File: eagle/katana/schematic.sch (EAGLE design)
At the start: 27 parts, among them IC1 MAX1044, Q1 2N5457, Q2 2N5457

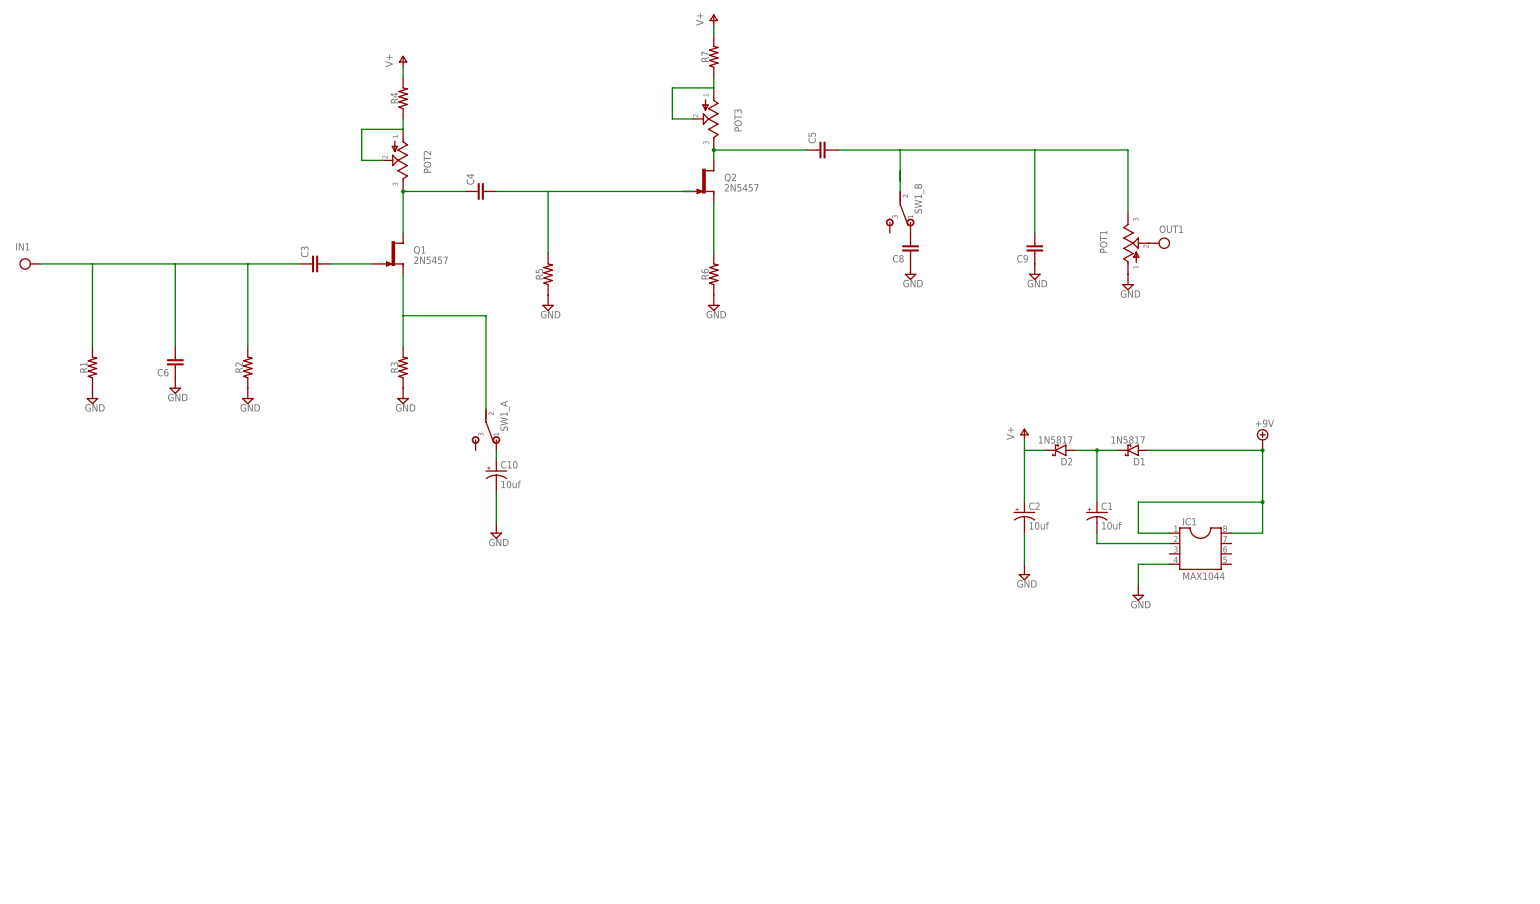
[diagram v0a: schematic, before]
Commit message: Se ha modificado esquematico y creado layout
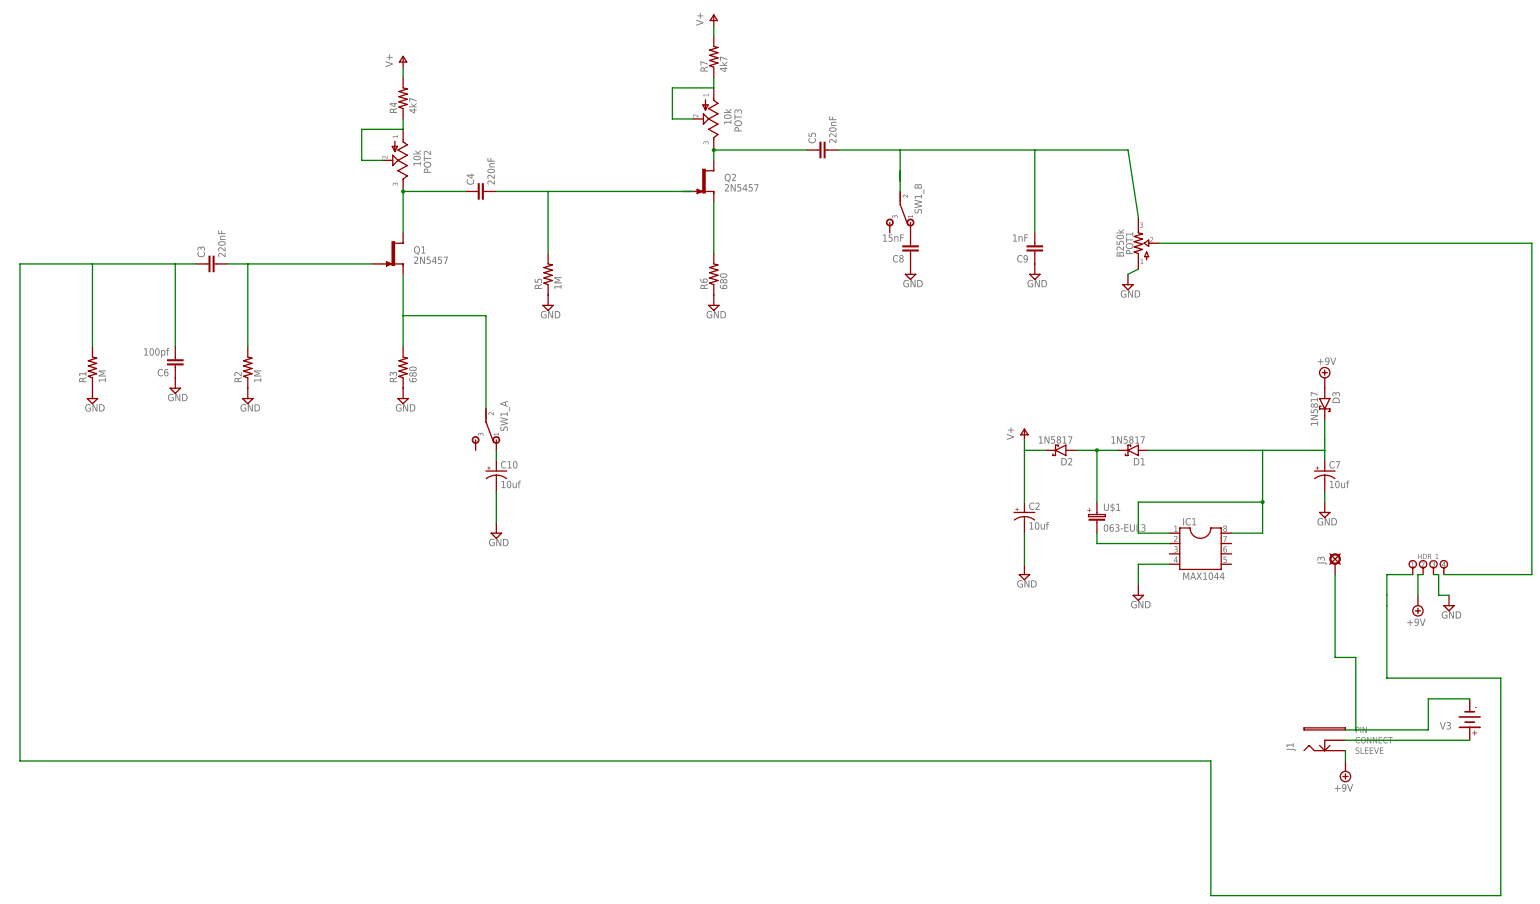
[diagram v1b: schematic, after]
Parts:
- removed C1: 10uf, gm-caps-electro-pol:0501
- removed IN1: IN(T), gm-supply:IN(T)
- removed OUT1: OUT(T), gm-supply:OUT(T)
- added C7: 10uf, gm-caps-electro-pol:0501
- added D3: 1N5817, gm-diodes:1N5817
- added HDR_1: 4PIN, headers:4PIN
- added J1: (no value), gm-jacks:DC
- added J3: (no value), gm-supply:PAD
- added U$1: 063-EUL3, gm-caps-electro-pol:063-EUL3
- added V3: (no value), supply pins:DC
- C3, C4, C5: value (none) -> 220nF
- C6: value (none) -> 100pf
- C8: value (none) -> 15nF
- C9: value (none) -> 1nF
- POT1: value (none) -> B250k; device gm-pots:POT -> potentiometers:16MM.1
- POT2, POT3: value (none) -> 10k
- R1, R2, R5: value (none) -> 1M; device resistors:R.3B -> gm-resistors:7MM
- R3, R6: value (none) -> 680; device resistors:R.3B -> gm-resistors:7MM
- R4, R7: value (none) -> 4k7; device resistors:R.3B -> gm-resistors:7MM
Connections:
- removed net IN: C3.1, C6.2, IN1.IN, R1.2, R2.2
- removed net OUT: OUT1.OUT, POT1.2
- new net N$15: J1.PIN, J3.PAD, V3.-
- new net N$16: C7.+, D1.A, D3.C, IC1.1, IC1.8
- new net N$17: C3.2, Q1.G, R2.2
- new net N$18: C3.1, C6.2, HDR_1.1, R1.2
- new net N$19: HDR_1.4, POT1.2
- net +9V: now also D3.A, HDR_1.2, J1.SLEEVE; no longer D1.A, IC1.1, IC1.8
- net GND: now also C7.-, HDR_1.3
- net N$1: now also U$1.-; no longer C1.-
- net N$2: now also U$1.+; no longer C1.+
- net N$3: now also J1.CONNECT, V3.+; no longer C3.2, Q1.G
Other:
- moved on the sheet: C3
